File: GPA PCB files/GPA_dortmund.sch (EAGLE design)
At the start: 167 parts, among them U10 INA149SOIC8, U100 AAVID_TO220_HEATSINK, U101 AAVID_TO220_HEATSINK, U102 AAVID_TO220_HEATSINK, U103 AAVID_TO220_HEATSINK, U11 OPA549_KV_11TO-220_11, U12 OPA549_KV_11TO-220_11, U13 INA149SOIC8, U17 OPA549_KV_11TO-220_11, U18 OPA549_KV_11TO-220_11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

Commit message: Revert "made ref voltage for OPA549 selectable via jumper (GND or 2.5 V)"
This reverts commit 30ad67fba3128f3ef77c4447bf5e5bf75d73f0cc.
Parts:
- removed SV6: (no value), con-lstb:MA03-1
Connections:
- removed net REF_OPA549: R29.2, R43.2, R71.2, R99.2, SV6.2
- net GND: no longer SV6.3
- net REF_2.5V: now also R29.2, R43.2, R71.2, R99.2; no longer SV6.1

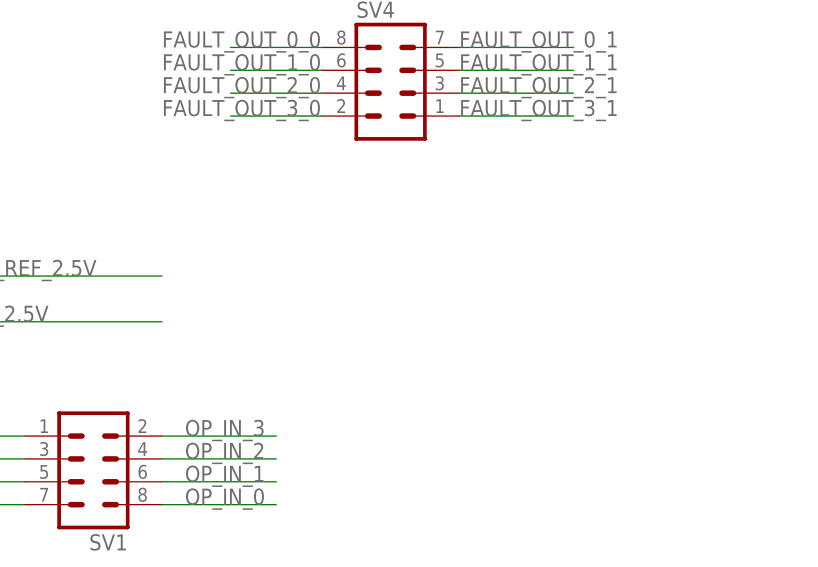
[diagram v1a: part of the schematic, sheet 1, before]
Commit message: made ref voltage for OPA549 selectable via jumper (GND or 2.5 V)
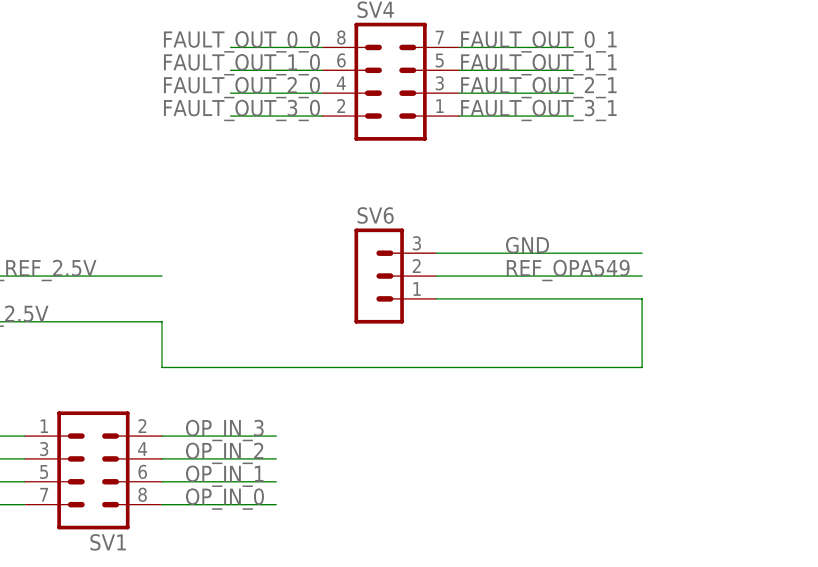
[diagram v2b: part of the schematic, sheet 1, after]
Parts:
- added SV6: (no value), con-lstb:MA03-1
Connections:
- new net REF_OPA549: R29.2, R43.2, R71.2, R99.2, SV6.2
- net GND: now also SV6.3
- net REF_2.5V: now also SV6.1; no longer R29.2, R43.2, R71.2, R99.2
